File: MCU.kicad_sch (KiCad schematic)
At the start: 54 parts, among them J1 GPS, J2 GPS, Q1 SI2301BDS, SW1 TS2306A, U4 RP2354B, U5 W25Q128JVPIQ, U6 TPD2E001DRLR, Y1 40MHz

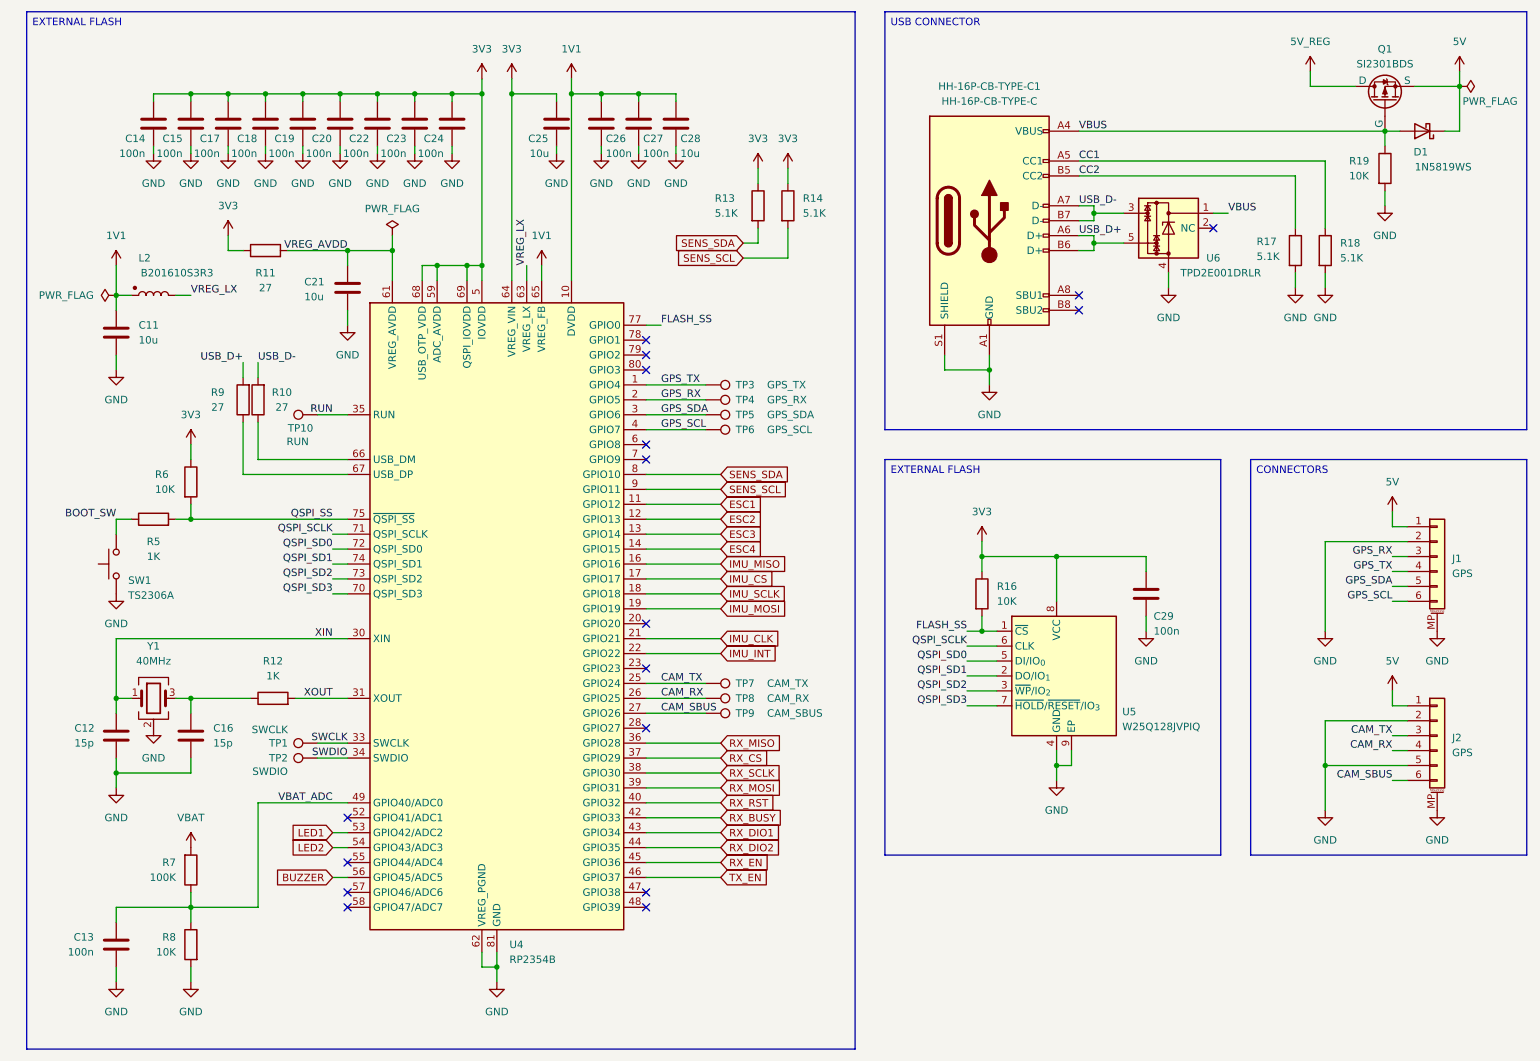
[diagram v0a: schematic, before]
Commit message: Connectors and tag
Added bulk capacitance for each ESC.
Added SWD connector.
Updated all tags.

TODO:
Add pads for the unconnected GPIO pins.
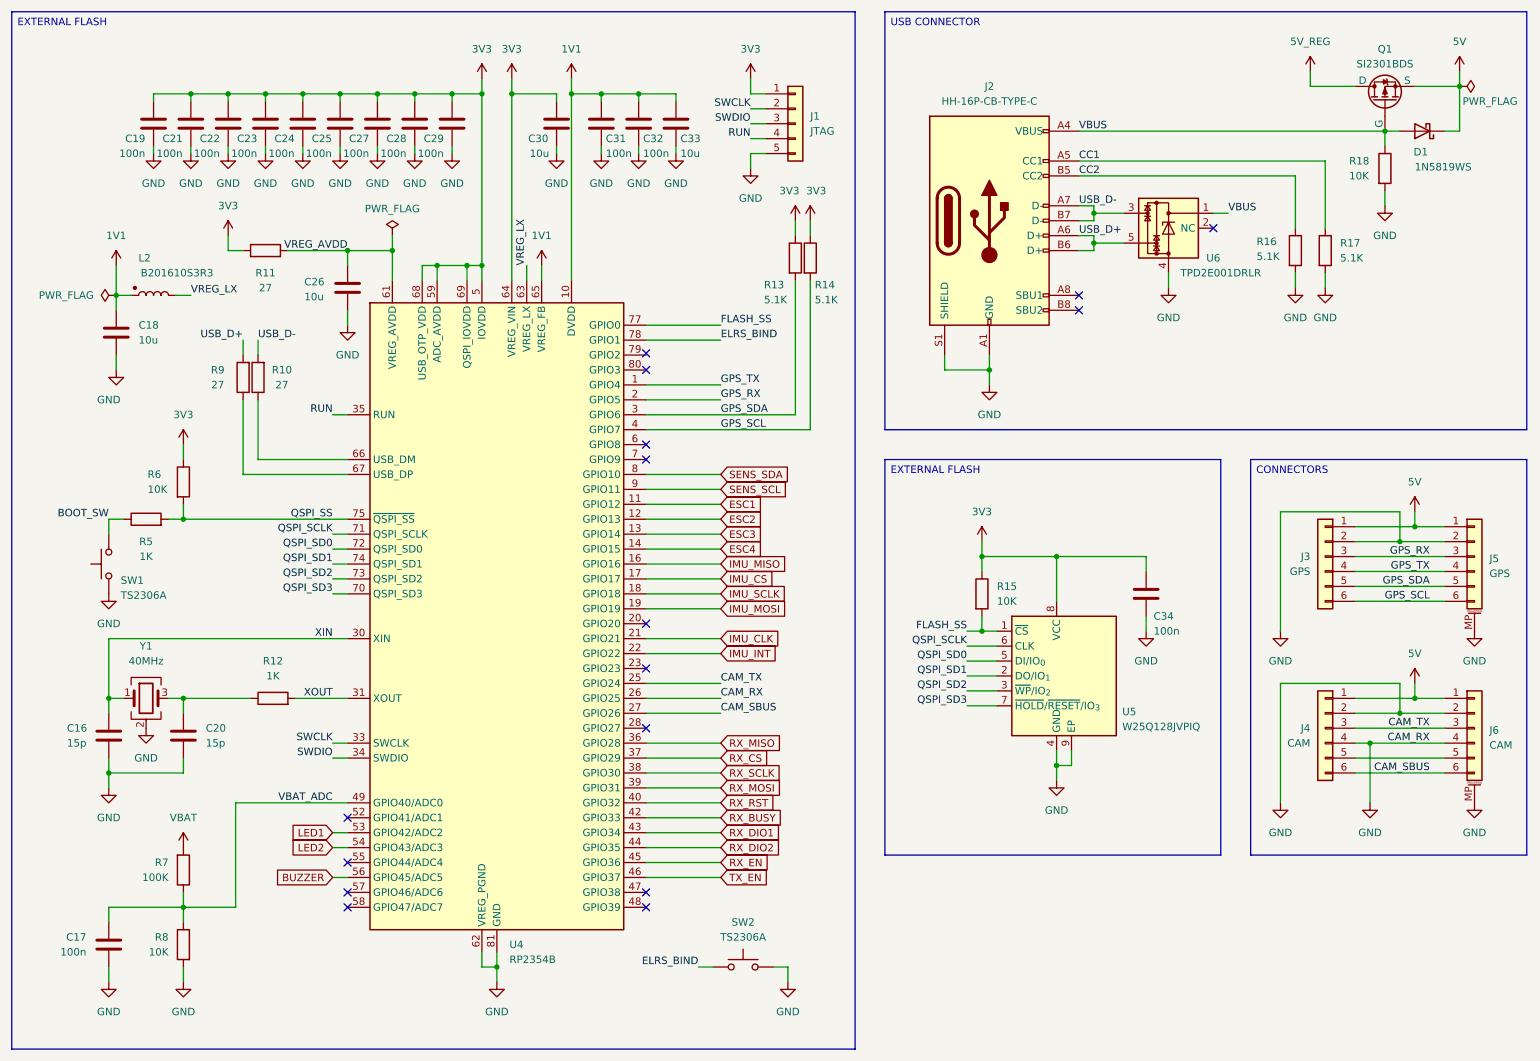
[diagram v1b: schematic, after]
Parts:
- removed HH-16P-CB-TYPE-C1: HH-16P-CB-TYPE-C, Custom_Parts:HH-16P-CB-TYPE-C, symbol Custom_Parts:HH-16P-CB-TYPE-C
- removed J2: GPS, Connector_JST:JST_SH_SM06B-SRSS-TB_1x06-1MP_P1.00mm_Horizontal, symbol Connector_Generic_MountingPin:Conn_01x06_MountingPin
- removed TP1: SWCLK, TestPoint:TestPoint_Pad_D1.0mm, symbol Connector:TestPoint
- removed TP10: RUN, TestPoint:TestPoint_Pad_D1.0mm, symbol Connector:TestPoint
- removed TP2: SWDIO, TestPoint:TestPoint_Pad_D1.0mm, symbol Connector:TestPoint
- removed TP3: GPS_TX, TestPoint:TestPoint_Pad_D1.0mm, symbol Connector:TestPoint
- removed TP4: GPS_RX, TestPoint:TestPoint_Pad_D1.0mm, symbol Connector:TestPoint
- removed TP5: GPS_SDA, TestPoint:TestPoint_Pad_D1.0mm, symbol Connector:TestPoint
- removed TP6: GPS_SCL, TestPoint:TestPoint_Pad_D1.0mm, symbol Connector:TestPoint
- removed TP7: CAM_TX, TestPoint:TestPoint_Pad_D1.0mm, symbol Connector:TestPoint
- removed TP8: CAM_RX, TestPoint:TestPoint_Pad_D1.0mm, symbol Connector:TestPoint
- removed TP9: CAM_SBUS, TestPoint:TestPoint_Pad_D1.0mm, symbol Connector:TestPoint
- added J1: JTAG, symbol Connector_Generic:Conn_01x05
- added J2: HH-16P-CB-TYPE-C, Custom_Parts:HH-16P-CB-TYPE-C, symbol Custom_Parts:HH-16P-CB-TYPE-C
- added J3: GPS, symbol Connector_Generic:Conn_01x06
- added J4: CAM, symbol Connector_Generic:Conn_01x06
- added J6: CAM, Connector_JST:JST_SH_SM06B-SRSS-TB_1x06-1MP_P1.00mm_Horizontal, symbol Connector_Generic_MountingPin:Conn_01x06_MountingPin
- added SW2: TS2306A, Custom_Parts:SW_SMD_3.0x2.0_PUSH, symbol Switch:SW_Push
- renumbered C12 to C16, C13 to C17, C11 to C18, C14 to C19, C16 to C20, C15 to C21, C17 to C22, C18 to C23, C19 to C24, C20 to C25, C21 to C26, C22 to C27, C23 to C28, C24 to C29, C25 to C30, C26 to C31, C27 to C32, C28 to C33, C29 to C34, J1 to J5, R16 to R15, R17 to R16, R18 to R17, R19 to R18
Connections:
- net CAM_RX is gone; now on net GND: U4.26 (GPIO25)
- net 3V3: now also J1.1 (Pin_1)
- net 5V: now also J3.1 (Pin_1), J4.1 (Pin_1), J6.1 (Pin_1)
- net CAM_SBUS: now also J4.6 (Pin_6), J6.6 (Pin_6)
- net CAM_TX: now also J4.3 (Pin_3), J6.3 (Pin_3)
- net CC1: now also J2.A5 (CC1)
- net CC2: now also J2.B5 (CC2)
- net GND: now also J1.5 (Pin_5), J2.A1 (GND), J2.B1 (GND), J2.S1 (SHIELD), J3.2 (Pin_2), J4.2 (Pin_2), J4.4 (Pin_4), J6.2 (Pin_2), J6.4 (Pin_4), J6.MP (MountPin), SW2.2
- net GPS_RX: now also J3.3 (Pin_3)
- net GPS_SCL: now also R14.2, J3.6 (Pin_6)
- net GPS_SDA: now also R13.2, J3.5 (Pin_5)
- net GPS_TX: now also J3.4 (Pin_4)
- net RUN: now also J1.4 (Pin_4)
- net SENS_SCL: no longer R14.2
- net SENS_SDA: no longer R13.2
- net SWCLK: now also J1.2 (Pin_2)
- net SWDIO: now also J1.3 (Pin_3)
- net USB_D+: now also J2.A6 (D+), J2.B6 (D+)
- net USB_D-: now also J2.A7 (D-), J2.B7 (D-)
- net VBUS: now also J2.A4 (VBUS), J2.B4 (VBUS)
- net ELRS_BIND: now reaches U4.78 (GPIO1)
- net ELRS_BIND: now also SW2.1
- new net: J4.5 (Pin_5), J6.5 (Pin_5)
- no-connect marks 17 -> 16
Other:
- moved on the sheet: C16, C17, C20, J5, R10, R13, R14, R5, R6, R7, R8, R9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

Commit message: Missing labels and revision
First complete revision of the schematic.
Added missing labels.

TODO:
Continue reviewing the schematic.
Include net coloring.
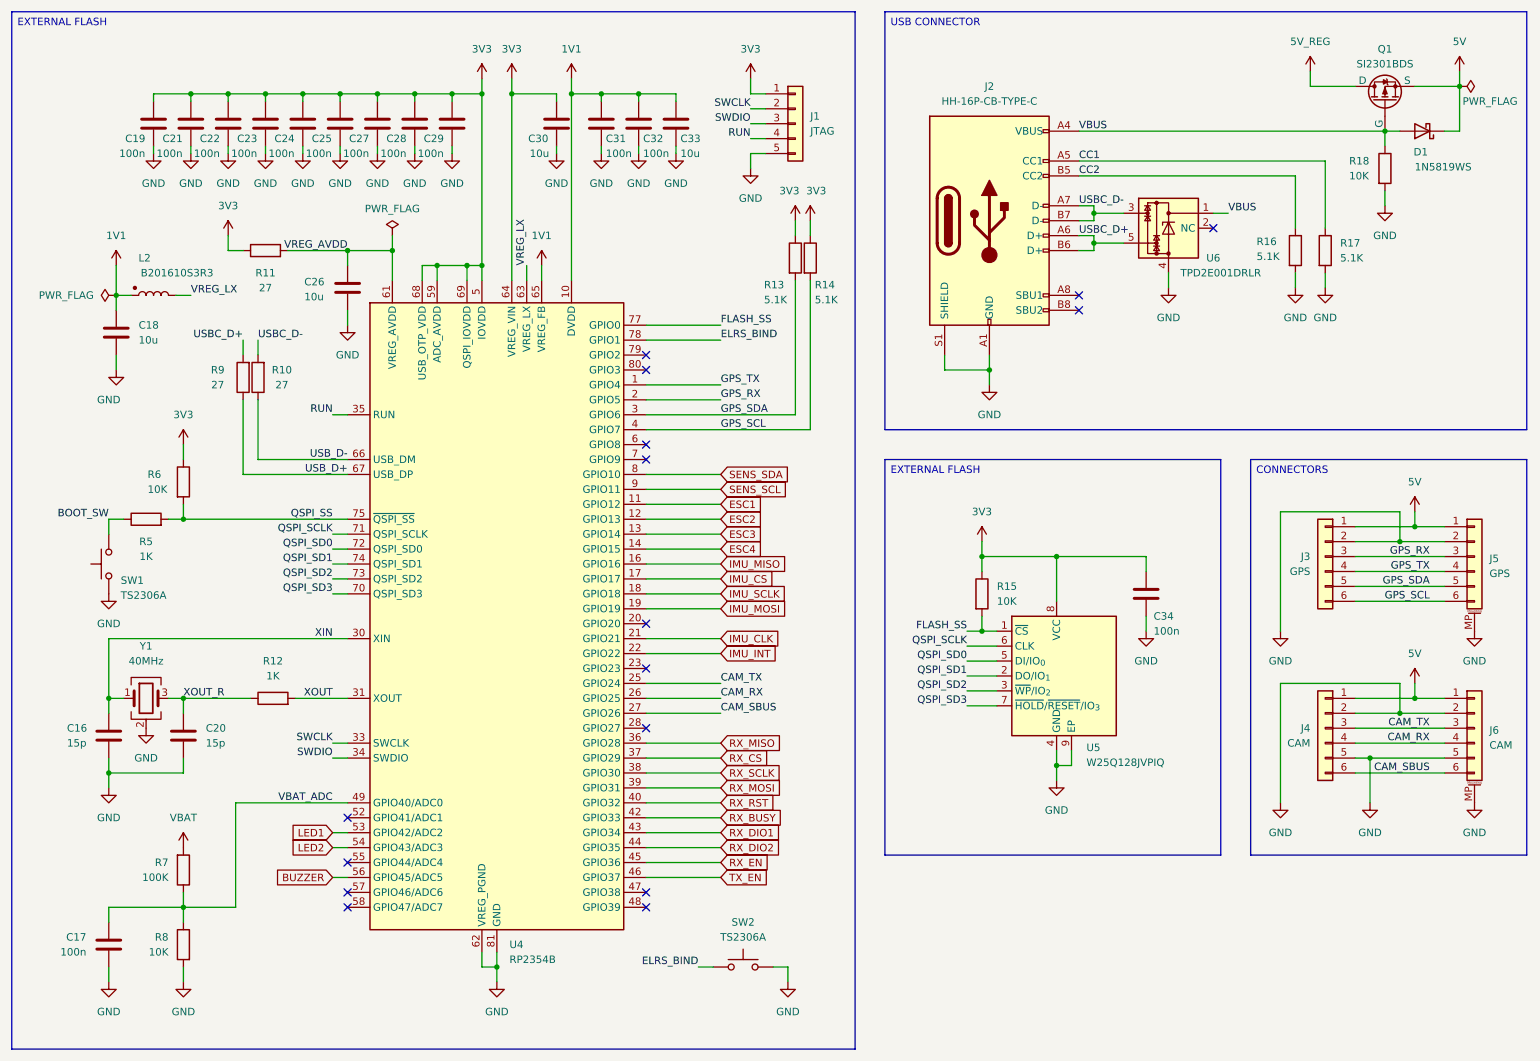
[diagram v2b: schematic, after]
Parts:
- C19, C20, C21, C22, C23, C24, C25: footprint Capacitor_SMD:C_0201_0603Metric -> Capacitor_SMD:C_0603_1608Metric
- J1: footprint (none) -> Custom_Parts:PAD_5_SQUARE_SOLID_1.0x1.0mm_P1.5mm
- J3, J4: footprint (none) -> Custom_Parts:PAD_6_SQUARE_SOLID_1.5x1.5mm_P2.0mm
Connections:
- net GND: now also J4.5 (Pin_5), J6.5 (Pin_5); no longer J4.4 (Pin_4), J6.4 (Pin_4), U4.26 (GPIO25)
- net USB_D+: now also R9.1, U4.67 (USB_DP); no longer J2.A6 (D+), J2.B6 (D+), R9.2, U6.5
- net USB_D-: now also R10.1, U4.66 (USB_DM); no longer J2.A7 (D-), J2.B7 (D-), R10.2, U6.3
- net XOUT_R: now reaches C20.1, R12.1, Y1.3
- new net CAM_RX: J4.4 (Pin_4), J6.4 (Pin_4), U4.26 (GPIO25)
- new net USBC_D+: J2.A6 (D+), J2.B6 (D+), R9.2, U6.5
- new net USBC_D-: J2.A7 (D-), J2.B7 (D-), R10.2, U6.3
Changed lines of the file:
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@@
 	)
 	(junction
-		(at 105.41 30.48)
+		(at 251.46 143.51)
 		(diameter 0)
 		(color 0 0 0 0)
 	)
 	(junction
-		(at 251.46 140.97)
+		(at 105.41 30.48)
 		(diameter 0)
 		(color 0 0 0 0)
@@
 	)
 	(no_connect
-		(at 128.27 74.6353)
+		(at 128.27 74.93)
 	)
 	(no_connect
@@
 	(wire
 		(pts
+			(xy 251.46 143.51) (xy 264.16 143.51)
+		)
+		(stroke
+			(width 0)
+			(type default)
+		)
+	)
+	(wire
+		(pts
 			(xy 128.27 156.21) (xy 140.97 156.21)
 		)
@@
 	(wire
 		(pts
+			(xy 251.46 143.51) (xy 251.46 151.13)
+		)
+		(stroke
+			(width 0)
+			(type default)
+		)
+	)
+	(wire
+		(pts
 			(xy 76.2 39.37) (xy 76.2 40.64)
 		)
@@
 	(wire
 		(pts
-			(xy 248.92 140.97) (xy 251.46 140.97)
+			(xy 248.92 140.97) (xy 264.16 140.97)
 		)
 		(stroke
@@
 	(wire
 		(pts
-			(xy 251.46 140.97) (xy 264.16 140.97)
-		)
-		(stroke
-			(width 0)
-			(type default)
-		)
-	)
-	(wire
-		(pts
 			(xy 204.47 49.53) (xy 204.47 50.8)
 		)
@@
 	(wire
 		(pts
-			(xy 248.92 143.51) (xy 264.16 143.51)
+			(xy 248.92 143.51) (xy 251.46 143.51)
 		)
 		(stroke
@@
 	(wire
 		(pts
-			(xy 251.46 140.97) (xy 251.46 151.13)
-		)
-		(stroke
-			(width 0)
-			(type default)
-		)
-	)
-	(wire
-		(pts
 			(xy 256.54 106.68) (xy 264.16 106.68)
 		)
@@
 		)
 	)
-	(label "USB_D+"
+	(label "USBC_D+"
 		(at 59.69 72.39 180)
 		(effects
@@
 		)
 	)
-	(label "USB_D-"
+	(label "XOUT_R"
+		(at 49.53 133.35 0)
+		(effects
+			(font
+				(size 1.27 1.27)
+			)
+			(justify left bottom)
+		)
+	)
+	(label "USBC_D-"
 		(at 201.93 49.53 0)
 		(effects
@@
 		)
 	)
-	(label "USB_D+"
+	(label "USBC_D+"
 		(at 201.93 54.61 0)
 		(effects
@@
 		)
 	)
-	(label "USB_D-"
+	(label "USBC_D-"
 		(at 62.23 72.39 0)
 		(effects
@@
 		)
 	)
+	(label "USB_D-"
+		(at 77.47 92.71 180)
+		(effects
+			(font
+				(size 1.27 1.27)
+			)
+			(justify right bottom)
+		)
+	)
 	(label "SWDIO"
 		(at 74.93 143.51 180)
@@
 		)
 	)
+	(label "USB_D+"
+		(at 77.47 95.25 180)
+		(effects
+			(font
+				(size 1.27 1.27)
+			)
+			(justify right bottom)
+		)
+	)
 	(label "GPS_TX"
 		(at 261.62 111.76 180)
@@
 			)
 		)
-		(property "Footprint" "Capacitor_SMD:C_0201_0603Metric"
+		(property "Footprint" "Capacitor_SMD:C_0603_1608Metric"
 			(at 77.1652 39.37 0)
 			(effects
@@
 		(dnp no)
 		(property "Reference" "U5"
-			(at 209.296 135.636 0)
+			(at 203.2 141.732 0)
 			(effects
 				(font
@@
 		)
 		(property "Value" "W25Q128JVPIQ"
-			(at 209.296 138.176 0)
+			(at 203.2 144.272 0)
 			(effects
 				(font
@@
 			)
 		)
-		(property "Footprint" "Capacitor_SMD:C_0201_0603Metric"
+		(property "Footprint" "Capacitor_SMD:C_0603_1608Metric"
 			(at 51.7652 39.37 0)
 			(effects
@@
 			)
 		)
-		(property "Footprint" "Capacitor_SMD:C_0201_0603Metric"
+		(property "Footprint" "Capacitor_SMD:C_0603_1608Metric"
 			(at 45.4152 39.37 0)
 			(effects
@@
 			)
 		)
-		(property "Footprint" ""
+		(property "Footprint" "Custom_Parts:PAD_6_SQUARE_SOLID_1.5x1.5mm_P2.0mm"
 			(at 243.84 109.22 0)
 			(effects
@@
 			)
 		)
-		(property "Footprint" ""
+		(property "Footprint" "Custom_Parts:PAD_5_SQUARE_SOLID_1.0x1.0mm_P1.5mm"
 			(at 153.67 35.56 0)
 			(effects
@@
 			)
 		)
-		(property "Footprint" "Capacitor_SMD:C_0201_0603Metric"
+		(property "Footprint" "Capacitor_SMD:C_0603_1608Metric"
 			(at 64.4652 39.37 0)
 			(effects
@@
 			)
 		)
-		(property "Footprint" "Capacitor_SMD:C_0201_0603Metric"
+		(property "Footprint" "Capacitor_SMD:C_0603_1608Metric"
 			(at 70.8152 39.37 0)
 			(effects
@@
 			)
 		)
-		(property "Footprint" "Capacitor_SMD:C_0201_0603Metric"
+		(property "Footprint" "Capacitor_SMD:C_0603_1608Metric"
 			(at 58.1152 39.37 0)
 			(effects
@@
 			)
 		)
-		(property "Footprint" "Capacitor_SMD:C_0201_0603Metric"
+		(property "Footprint" "Capacitor_SMD:C_0603_1608Metric"
 			(at 50.4952 143.51 0)
 			(effects
@@
 			)
 		)
-		(property "Footprint" ""
+		(property "Footprint" "Custom_Parts:PAD_6_SQUARE_SOLID_1.5x1.5mm_P2.0mm"
 			(at 243.84 138.43 0)
 			(effects

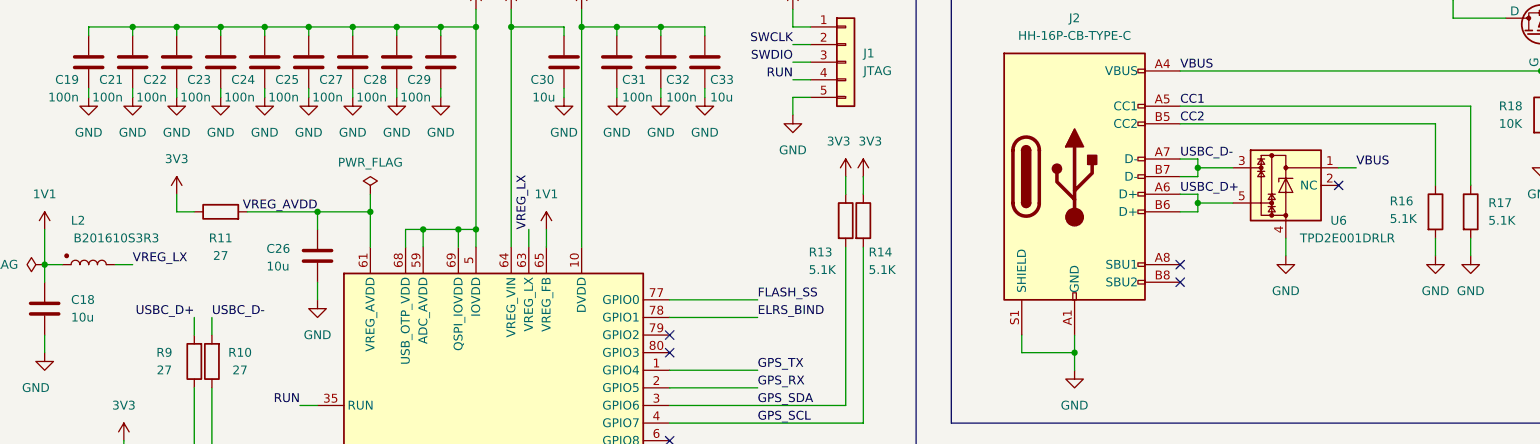
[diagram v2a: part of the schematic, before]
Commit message: Board outline and net nodes
Added an initial board outline.
Updated net nodes definitions.
Updated board rules for manufacturing.
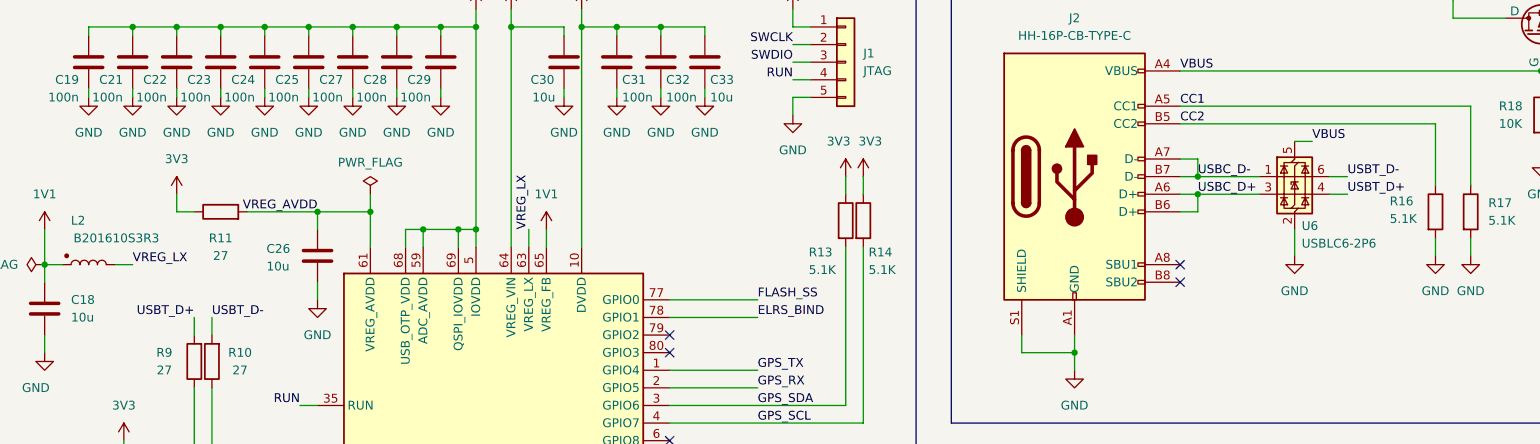
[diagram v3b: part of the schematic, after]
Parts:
- removed U6: TPD2E001DRLR, Package_TO_SOT_SMD:SOT-553, symbol Custom_Parts:TPD2E001DRLR
- added U6: USBLC6-2P6, Package_TO_SOT_SMD:SOT-666, symbol Power_Protection:USBLC6-2P6
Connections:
- net GND: now also U6.2 (GND)
- net USBC_D+: now also U6.3 (I/O2); no longer R9.2
- net USBC_D-: now also U6.1 (I/O1); no longer R10.2
- net VBUS: now also U6.5 (VBUS)
- new net USBT_D+: R9.2, U6.4 (I/O2)
- new net USBT_D-: R10.2, U6.6 (I/O1)
- no-connect marks 16 -> 15
